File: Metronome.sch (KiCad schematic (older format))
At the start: 30 parts, among them CON1 PDI_50mil, IC1 ATXMEGA8E5-MU, P1 USB_B, Q1 Q_PMOS_GSD, U1 AS1117, U2 NCP706A

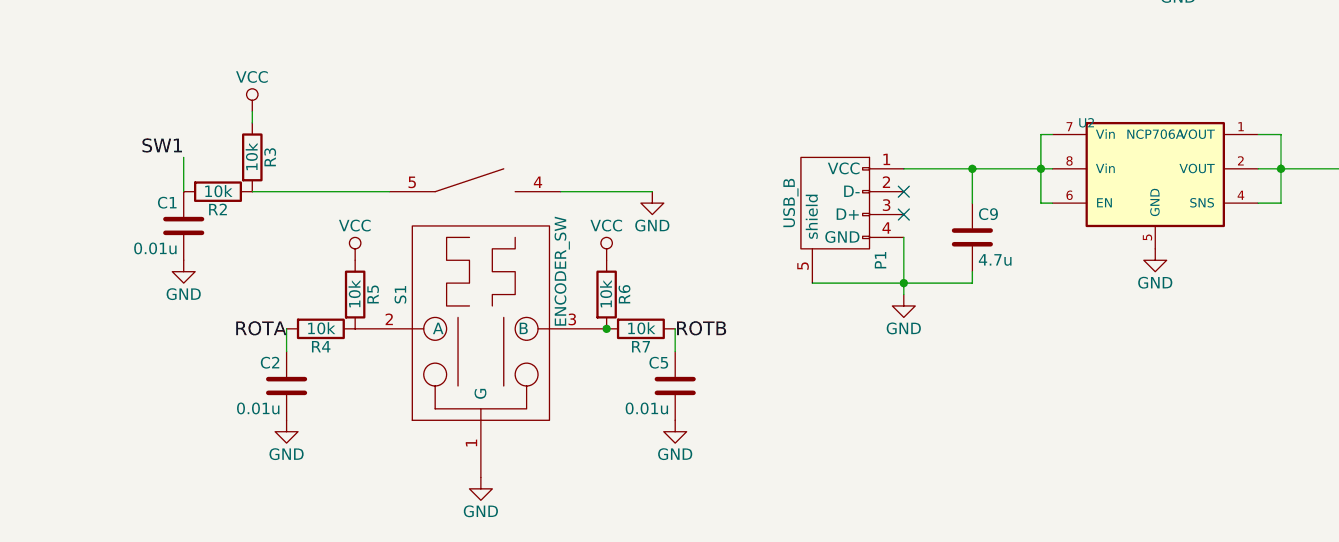
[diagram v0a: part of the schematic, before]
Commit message: Set proper pin direction to fix ERC errors.
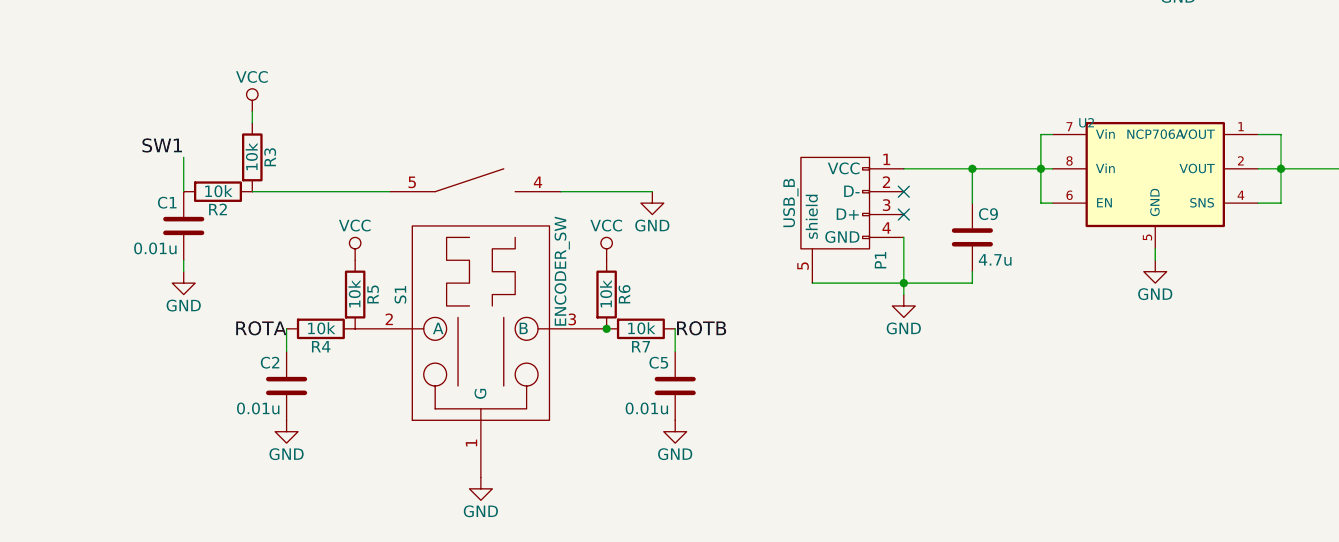
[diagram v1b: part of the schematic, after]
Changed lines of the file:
@@
 LIBS:power
 LIBS:device
-LIBS:transistors
 LIBS:conn
-LIBS:audio
 LIBS:atmel
-LIBS:contrib
 LIBS:ams
 LIBS:encoder
@@
 LIBS:7segment_3digits
 LIBS:pdi_50mil
-LIBS:74xgxx
-LIBS:pspice
 LIBS:Metronome-cache
 EELAYER 25 0
@@
 	-1   0    0    -1
 $EndComp
-$Comp
-L GND #PWR016
-U 1 1 562CAA33
-P 1450 6150
-F 0 "#PWR016" H 1450 5900 50  0001 C CNN
-F 1 "GND" H 1450 6000 50  0000 C CNN
-F 2 "" H 1450 6150 60  0000 C CNN
-F 3 "" H 1450 6150 60  0000 C CNN
-	1    1450 6150
-	1    0    0    -1
-$EndComp
 Text Label 1450 5700 2    60   ~ 0
 SW1
@@
 	1450 5700 1450 5850
 $Comp
-L VCC #PWR017
+L VCC #PWR016
 U 1 1 562CB4A8
 P 1750 5500
-F 0 "#PWR017" H 1750 5350 50  0001 C CNN
+F 0 "#PWR016" H 1750 5350 50  0001 C CNN
 F 1 "VCC" H 1750 5650 50  0000 C CNN
 F 2 "" H 1750 5500 60  0000 C CNN
@@
 	6150 5750 6800 5750
 $Comp
-L GND #PWR018
+L GND #PWR017
 U 1 1 562CC9EE
 P 6800 6050
-F 0 "#PWR018" H 6800 5800 50  0001 C CNN
+F 0 "#PWR017" H 6800 5800 50  0001 C CNN
 F 1 "GND" H 6800 5900 50  0000 C CNN
 F 2 "" H 6800 6050 60  0000 C CNN
@@
 $EndComp
 $Comp
-L GND #PWR019
+L GND #PWR018
 U 1 1 562CCA36
-P 5700 6100
-F 0 "#PWR019" H 5700 5850 50  0001 C CNN
-F 1 "GND" H 5700 5950 50  0000 C CNN
-F 2 "" H 5700 6100 60  0000 C CNN
-F 3 "" H 5700 6100 60  0000 C CNN
-	1    5700 6100
-	1    0    0    -1
-$EndComp
-$Comp
-L VCC #PWR020
+P 5700 6150
+F 0 "#PWR018" H 5700 5900 50  0001 C CNN
+F 1 "GND" H 5700 6000 50  0000 C CNN
+F 2 "" H 5700 6150 60  0000 C CNN
+F 3 "" H 5700 6150 60  0000 C CNN
+	1    5700 6150
+	1    0    0    -1
+$EndComp
+$Comp
+L VCC #PWR019
 U 1 1 562CCB75
 P 6800 5700
-F 0 "#PWR020" H 6800 5550 50  0001 C CNN
+F 0 "#PWR019" H 6800 5550 50  0001 C CNN
 F 1 "VCC" H 6800 5850 50  0000 C CNN
 F 2 "" H 6800 5700 60  0000 C CNN
@@
 	1300 1500 1300 1550
 $Comp
-L GND #PWR021
+L GND #PWR020
 U 1 1 562FCD54
 P 1300 1550
-F 0 "#PWR021" H 1300 1300 50  0001 C CNN
+F 0 "#PWR020" H 1300 1300 50  0001 C CNN
 F 1 "GND" H 1300 1400 50  0000 C CNN
 F 2 "" H 1300 1550 60  0000 C CNN
@@
 $EndComp
 $Comp
-L VCC #PWR022
+L VCC #PWR021
 U 1 1 562FCE65
 P 1250 1050
-F 0 "#PWR022" H 1250 900 50  0001 C CNN
+F 0 "#PWR021" H 1250 900 50  0001 C CNN
 F 1 "VCC" H 1250 1200 50  0000 C CNN
 F 2 "" H 1250 1050 60  0000 C CNN
@@
 	4300 1950 4300 2100
 $Comp
-L GND #PWR023
+L GND #PWR022
 U 1 1 56301C4B
 P 4300 2100
-F 0 "#PWR023" H 4300 1850 50  0001 C CNN
+F 0 "#PWR022" H 4300 1850 50  0001 C CNN
 F 1 "GND" H 4300 1950 50  0000 C CNN
 F 2 "" H 4300 2100 60  0000 C CNN
@@
 $EndComp
 $Comp
-L VCC #PWR024
+L VCC #PWR023
 U 1 1 56301CB3
 P 4300 1100
-F 0 "#PWR024" H 4300 950 50  0001 C CNN
+F 0 "#PWR023" H 4300 950 50  0001 C CNN
 F 1 "VCC" H 4300 1250 50  0000 C CNN
 F 2 "" H 4300 1100 60  0000 C CNN
@@
 	4600 6050 4600 6300
 $Comp
-L GND #PWR025
+L GND #PWR024
 U 1 1 56302C09
 P 4600 6300
-F 0 "#PWR025" H 4600 6050 50  0001 C CNN
+F 0 "#PWR024" H 4600 6050 50  0001 C CNN
 F 1 "GND" H 4600 6150 50  0000 C CNN
 F 2 "" H 4600 6300 60  0000 C CNN
@@
 Wire Wire Line
 	6250 5900 6150 5900
+Wire Wire Line
+	5700 6150 5700 6100
+$Comp
+L GND #PWR025
+U 1 1 56328047
+P 1450 6200
+F 0 "#PWR025" H 1450 5950 50  0001 C CNN
+F 1 "GND" H 1450 6050 50  0000 C CNN
+F 2 "" H 1450 6200 60  0000 C CNN
+F 3 "" H 1450 6200 60  0000 C CNN
+	1    1450 6200
+	1    0    0    -1
+$EndComp
+Wire Wire Line
+	1450 6200 1450 6150
 $EndSCHEMATC

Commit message: Optimize layout to fit buzzer on board. Add ID pin to USB micro B connector.
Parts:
- P1: footprint Connect:USB_Micro-B -> footprints:USB_Micro-B_smd; symbol USB_B -> USB_micro_B
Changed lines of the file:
@@
 LIBS:7segment_3digits
 LIBS:pdi_50mil
+LIBS:usb
 LIBS:Metronome-cache
 EELAYER 25 0
@@
 NoConn ~ 3800 2600
 NoConn ~ 3800 2800
-NoConn ~ 3800 2900
 NoConn ~ 3800 3000
 NoConn ~ 3800 3100
@@
 	4300 1100 4300 1150
 Wire Wire Line
-	4000 1350 4000 2700
-Wire Wire Line
-	4000 2700 3800 2700
-$Comp
-L USB_B P1
+	4000 1350 4000 2900
+$Comp
+L USB_micro_B P1
 U 1 1 5630275D
 P 4300 5950
 F 0 "P1" H 4500 5750 50  0000 C CNN
 F 1 "USB_B" H 4250 6150 50  0000 C CNN
-F 2 "Connect:USB_Micro-B" V 4250 5850 60  0001 C CNN
+F 2 "footprints:USB_Micro-B_smd" V 4250 5850 60  0001 C CNN
 F 3 "" V 4250 5850 60  0000 C CNN
 F 4 "FCI" H 4300 5950 60  0001 C CNN "MFN"
@@
 $EndComp
 Wire Wire Line
-	4600 6050 4600 6300
+	4600 6050 4600 6500
 $Comp
 L GND #PWR024
 U 1 1 56302C09
-P 4600 6300
-F 0 "#PWR024" H 4600 6050 50  0001 C CNN
-F 1 "GND" H 4600 6150 50  0000 C CNN
-F 2 "" H 4600 6300 60  0000 C CNN
-F 3 "" H 4600 6300 60  0000 C CNN
-	1    4600 6300
-	1    0    0    -1
-$EndComp
-Wire Wire Line
-	4200 6250 4900 6250
-Connection ~ 4600 6250
+P 4600 6500
+F 0 "#PWR024" H 4600 6250 50  0001 C CNN
+F 1 "GND" H 4600 6350 50  0000 C CNN
+F 2 "" H 4600 6500 60  0000 C CNN
+F 3 "" H 4600 6500 60  0000 C CNN
+	1    4600 6500
+	1    0    0    -1
+$EndComp
+Wire Wire Line
+	4200 6350 4900 6350
+Connection ~ 4600 6350
 Wire Wire Line
 	4600 5750 5250 5750
@@
 Connection ~ 4900 5750
 Wire Wire Line
-	4900 6250 4900 6200
+	4900 6350 4900 6200
 $Comp
 L R R11
@@
 Wire Wire Line
 	1450 6200 1450 6150
+Wire Wire Line
+	4000 2900 3800 2900
+NoConn ~ 3800 2700
+Connection ~ 4600 6150
 $EndSCHEMATC

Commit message: Add 32kHz crystal to XMega circuit.
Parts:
- added Y1: Crystal, footprints:crystal_ABS05_Abracon_smd, symbol Crystal
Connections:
- wire segments 92 -> 96
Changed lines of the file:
@@
 NoConn ~ 3800 2700
 Connection ~ 4600 6150
+$Comp
+L Crystal Y1
+U 1 1 5633897E
+P 850 3000
+F 0 "Y1" H 850 3150 50  0000 C CNN
+F 1 "Crystal" H 850 2850 50  0000 C CNN
+F 2 "footprints:crystal_ABS05_Abracon_smd" H 850 3000 60  0001 C CNN
+F 3 "" H 850 3000 60  0000 C CNN
+F 4 "Abracon" H 850 3000 60  0001 C CNN "MFN"
+F 5 "ABS05-32.768KHZ-T" H 850 3000 60  0001 C CNN "MFP"
+	1    850  3000
+	0    1    1    0
+$EndComp
+Wire Wire Line
+	850  2850 1150 2850
+Wire Wire Line
+	1150 2850 1150 3000
+Wire Wire Line
+	850  3150 1150 3150
+Wire Wire Line
+	1150 3150 1150 3100
 $EndSCHEMATC
